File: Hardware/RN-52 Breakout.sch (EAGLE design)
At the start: 13 parts, among them U1 BLUETOOTH-RN-52

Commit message: Added Version
Added Version and cleaned up repo
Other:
- note added: "V10"
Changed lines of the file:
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@@
 <sheet>
 <plain>
-<text x="166.624" y="11.684" size="1.778" layer="91">Joel B</text>
+<text x="166.624" y="9.144" size="5.08" layer="96">Joel B</text>
+<text x="238.76" y="7.62" size="2.54" layer="96">V10</text>
 </plain>
 <instances>

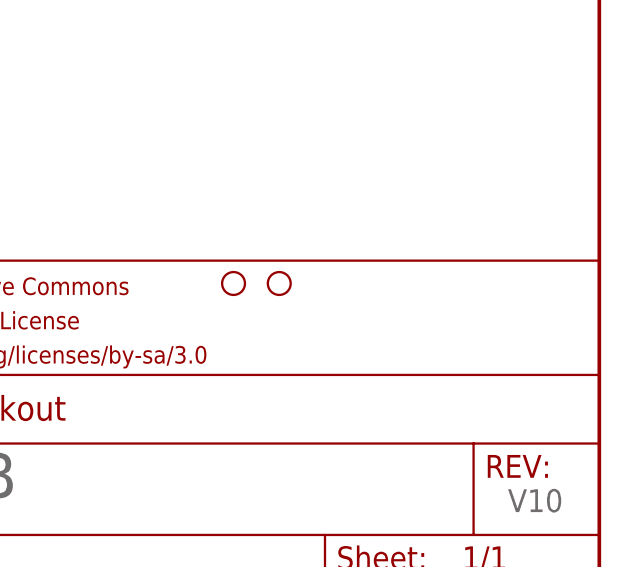
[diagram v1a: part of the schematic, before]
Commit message: added local fiducials
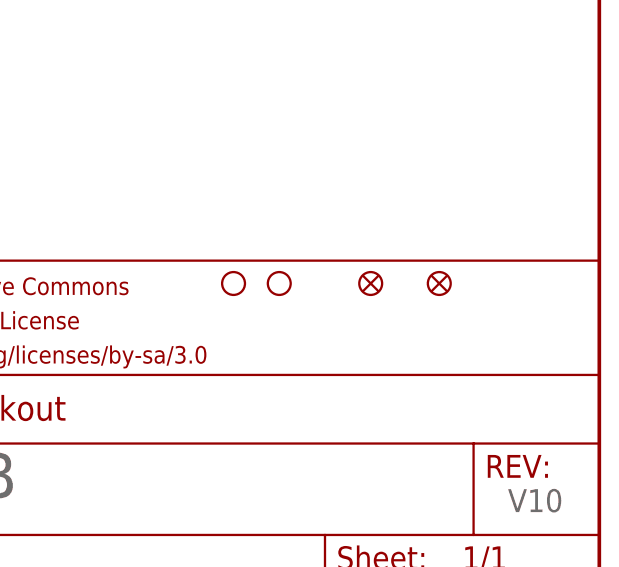
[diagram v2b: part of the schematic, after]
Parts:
- added FID1, FID2: FIDUCIAL1X2, SparkFun-Aesthetics:FIDUCIAL1X2
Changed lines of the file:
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@@
 <?xml version="1.0" encoding="utf-8"?>
 <!DOCTYPE eagle SYSTEM "eagle.dtd">
-<eagle version="6.4">
+<eagle version="6.5.0">
 <drawing>
 <settings>
@@
 <layer number="91" name="Nets" color="2" fill="1" visible="yes" active="yes"/>
 <layer number="92" name="Busses" color="1" fill="1" visible="yes" active="yes"/>
-<layer number="93" name="Pins" color="2" fill="1" visible="no" active="yes"/>
+<layer number="93" name="Pins" color="2" fill="1" visible="yes" active="yes"/>
 <layer number="94" name="Symbols" color="4" fill="1" visible="yes" active="yes"/>
 <layer number="95" name="Names" color="7" fill="1" visible="yes" active="yes"/>
@@
 <layer number="144" name="Drill_legend" color="7" fill="1" visible="yes" active="yes"/>
 <layer number="151" name="HeatSink" color="7" fill="1" visible="yes" active="yes"/>
-<layer number="199" name="Contour" color="7" fill="1" visible="no" active="yes"/>
+<layer number="199" name="Contour" color="7" fill="1" visible="yes" active="yes"/>
 <layer number="200" name="200bmp" color="1" fill="10" visible="yes" active="yes"/>
 <layer number="201" name="201bmp" color="2" fill="10" visible="yes" active="yes"/>
@@
 <part name="STANDOFF1" library="SparkFun-Electromechanical" deviceset="STAND-OFF" device=""/>
 <part name="STANDOFF2" library="SparkFun-Electromechanical" deviceset="STAND-OFF" device=""/>
+<part name="FID1" library="SparkFun-Aesthetics" deviceset="FIDUCIAL" device="1X2"/>
+<part name="FID2" library="SparkFun-Aesthetics" deviceset="FIDUCIAL" device="1X2"/>
 </parts>
 <sheets>
@@
 <instance part="STANDOFF1" gate="G$1" x="208.28" y="33.02"/>
 <instance part="STANDOFF2" gate="G$1" x="213.36" y="33.02"/>
+<instance part="FID1" gate="G$1" x="223.52" y="33.02"/>
+<instance part="FID2" gate="G$1" x="231.14" y="33.02"/>
 </instances>
 <busses>
